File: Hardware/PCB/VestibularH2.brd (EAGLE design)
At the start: 58 x 52.5 mm, 84 parts, among them IC1 FT232RL, IC10 THS4281DBVT, IC11 SN74LVC1G125DBVT, IC12 SN74LVC1G125DBVT, IC2 SN74LVC1G125DBVT, IC3 LP5907MFX-3.3, IC7 USBLC6-2SC6, IC8 ATXMEGA32A4U, IC9 LP5907MFX-3.3, T1 DMG1012UW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

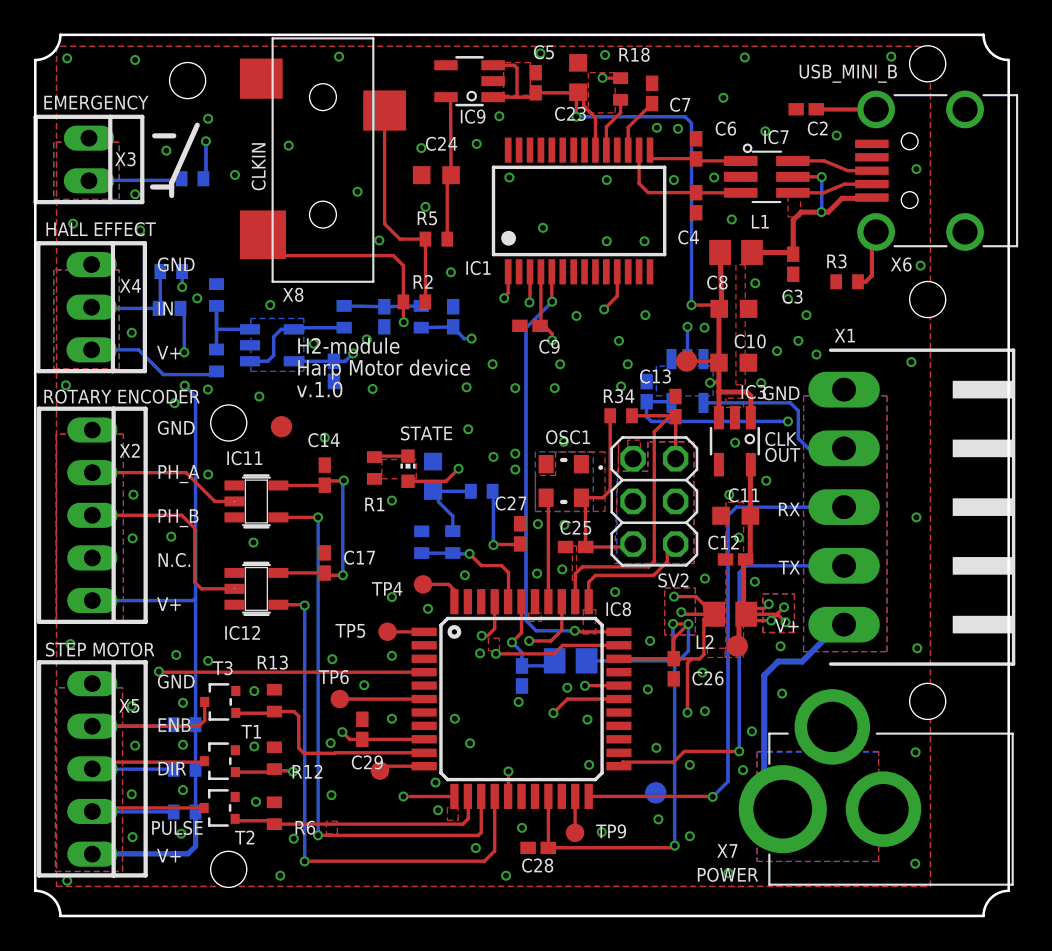
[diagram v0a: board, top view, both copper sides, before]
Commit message: Replaced files with PCB version 1.1.
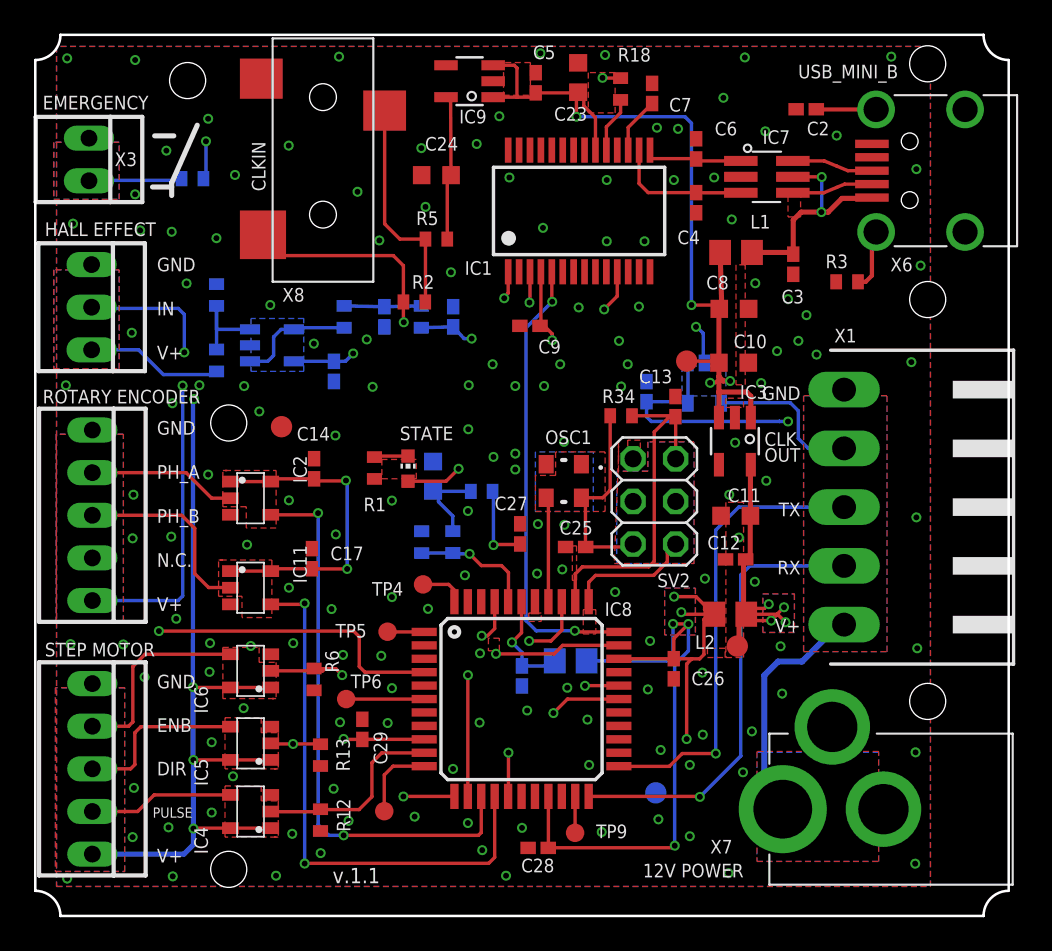
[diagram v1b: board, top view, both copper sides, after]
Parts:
- removed R10: DNI 0R, Harp Motor H2-module v1.0:R0402
- removed R11: 0R, Harp Motor H2-module v1.0:R0402
- removed R14, R15, R16: DNI, Harp Motor H2-module v1.0:R0402
- removed T1, T2, T3: DMG1012UW, Harp Motor H2-module v1.0:SOT323
- added IC4, IC5, IC6: M74VHC1GT126DT1G, Harp Motor H2-module v1.0:TSOP-5
- C15: value DNI 4.7uF -> DNI
- IC11, IC12, IC2: value SN74LVC1G125DBVT -> M74VHC1GT126DT1G; device Harp Motor H2-module v1.0:SOT23-5 -> Harp Motor H2-module v1.0:TSOP-5
- R9: value DNI 100R -> DNI
- moved IC12 29.4 mm to (39.9, 31.8), flipped to the bottom, turned to 180 degrees
- moved IC2 27.0 mm to (12.8, 24.9), flipped to the top, turned to 270 degrees
- moved R6 8.32 mm to (16.6, 14.1), turned to 90 degrees
- moved IC11 5.15 mm to (12.8, 19.6)
- moved R12 4.60 mm to (17.0, 5.71), turned to 90 degrees
- moved R13 4.25 mm to (17.0, 9.59), turned to 90 degrees
- moved TP8 2.43 mm to (20.8, 6.24)
- moved C17 0.80 mm to (16.5, 21.3)
- moved C14 0.74 mm to (16.6, 26.6)
- moved TP6 0.38 mm to (18.5, 12.9)
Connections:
- removed net N$51: R10.1, R11.1, X4.2
- net +3V3: now also IC11.1, IC12.1, IC2.1; no longer R11.2
- net +5V: now also IC4.1, IC4.5, IC5.1, IC5.5, IC6.1, IC6.5, X4.2; no longer R10.2, R14.2, R15.2, R16.2
- net ENCODER_A_PHASE: now also IC11.2; no longer IC12.2
- net ENCODER_B_PHASE: now also IC2.2; no longer IC11.2
- net GND: now also IC4.3, IC5.3, IC6.3; no longer IC11.1, IC12.1, IC2.1, T1.2, T2.2, T3.2
- net HARP_H2_CLOCK_OUT: now also IC12.4; no longer IC2.4
- net HARP_H2_RX: now also X1.2; no longer X1.3
- net HARP_H2_TX: now also X1.3; no longer X1.2
- net STEP_DIRECTION: now also IC5.4; no longer R15.1, T1.3
- net STEP_ENABLE: now also IC6.4; no longer R14.1, T3.3
- net STEP_PULSE: now also IC4.4; no longer R16.1, T2.3
- net U_CLOCK_IN: now also IC12.2; no longer IC2.2
- net U_ENCODER_A_PHASE: now also IC11.4; no longer IC12.4
- net U_ENCODER_B_PHASE: now also IC2.4; no longer IC11.4
- net U_STEP_DIRECTION: now also IC5.2, R13.2; no longer R12.2, T1.1
- net U_STEP_ENABLE: now also IC6.2, IC8.13, R6.2; no longer IC8.10, R13.2, T3.1
- net U_STEP_PULSE: now also IC4.2, IC8.10, R12.2; no longer IC8.13, R6.2, T2.1
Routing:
- net +5V: track 126.6 -> 188.7 mm, vias 5 -> 10
- net +3V3: track 230.7 -> 202.3 mm, vias 16 -> 15
- net U_STEP_ENABLE: track 13.4 -> 19.8 mm, vias 0 -> 2
- net N$51: track 6.27 -> 0.00 mm
- net HARP_H2_RX: track 31.7 -> 27.2 mm
- net U_STEP_PULSE: track 15.5 -> 12.1 mm
- net STEP_PULSE: track 11.7 -> 8.64 mm
- net HARP_H2_TX: track 24.6 -> 27.6 mm
- net N$17: track 2.74 -> 4.75 mm
- net STEP_DIRECTION: track 11.8 -> 10.4 mm
- net HARP_H2_CLOCK_OUT: track 10.5 -> 9.44 mm
- net U_ENCODER_A_PHASE: track 31.7 -> 32.7 mm
- net U_CLOCK_IN: track 63.0 -> 64.0 mm
- net STEP_ENABLE: track 12.8 -> 11.9 mm
- net U_STEP_DIRECTION: track 17.9 -> 18.6 mm
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- added copper zone on layer 1, net X1
- added copper zone on layer 1, net X2
- added copper zone on layer 1, net X3
- added copper zone on layer 1, net X4
- added copper zone on layer 1, net X5
- removed copper zone on layer 1, net N$59
- removed copper zone on layer 1, net N$61
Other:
- board text added: "12V POWER"
- board text added: "GND TX RX V+"
- board text added: "v.1.1"
- board text removed: "GND RX TX V+"
- board text removed: "H2-module Harp Motor device v.1.0"
- board text removed: "POWER"
